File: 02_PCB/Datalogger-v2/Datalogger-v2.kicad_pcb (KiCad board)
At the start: 2 copper layers, 140 x 90 mm, 23 parts, among them U1 Micro SD Card Adapter, U7 TP4056, U8 ESP32 DEV KIT DOIT

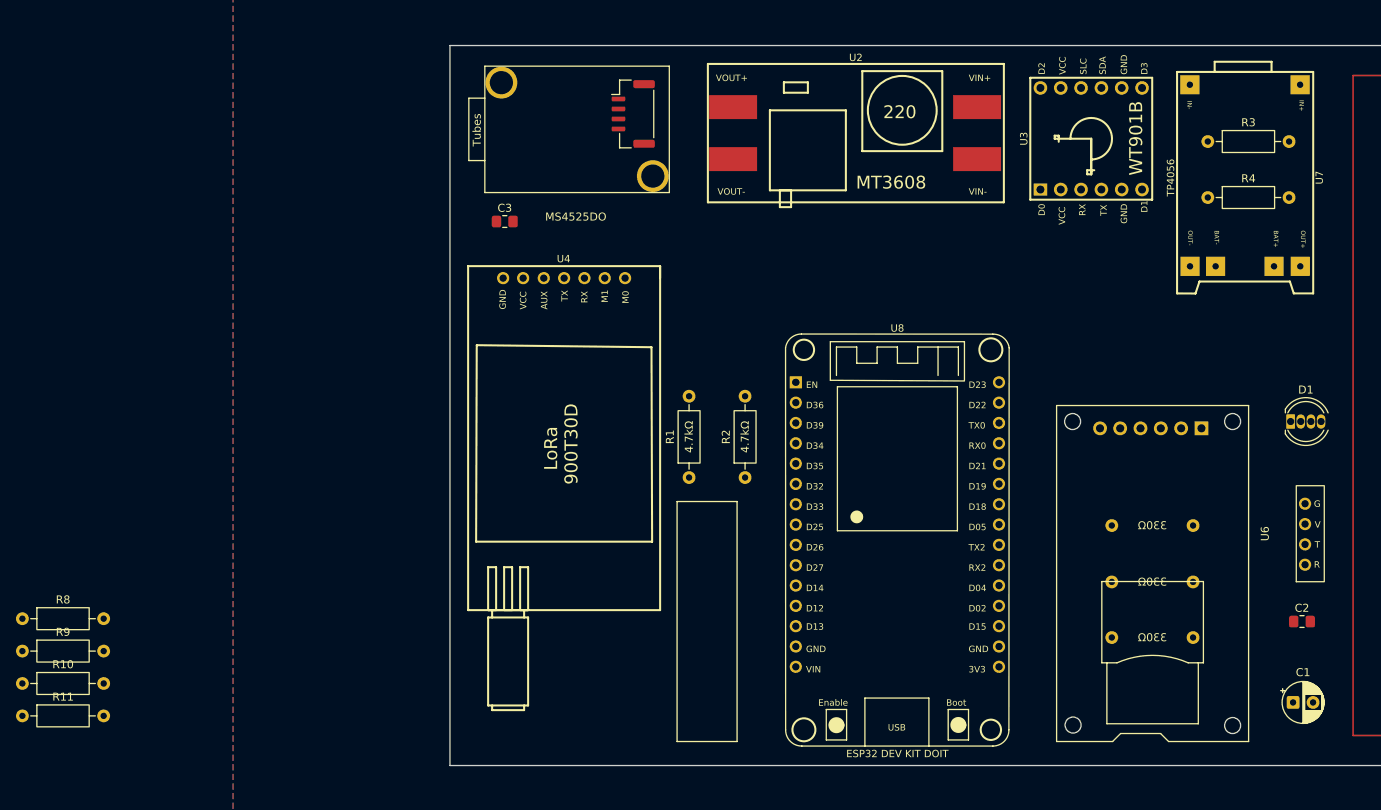
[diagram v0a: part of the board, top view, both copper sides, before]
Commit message: Update schematic and PCB files
- Add symbol and footprint library.
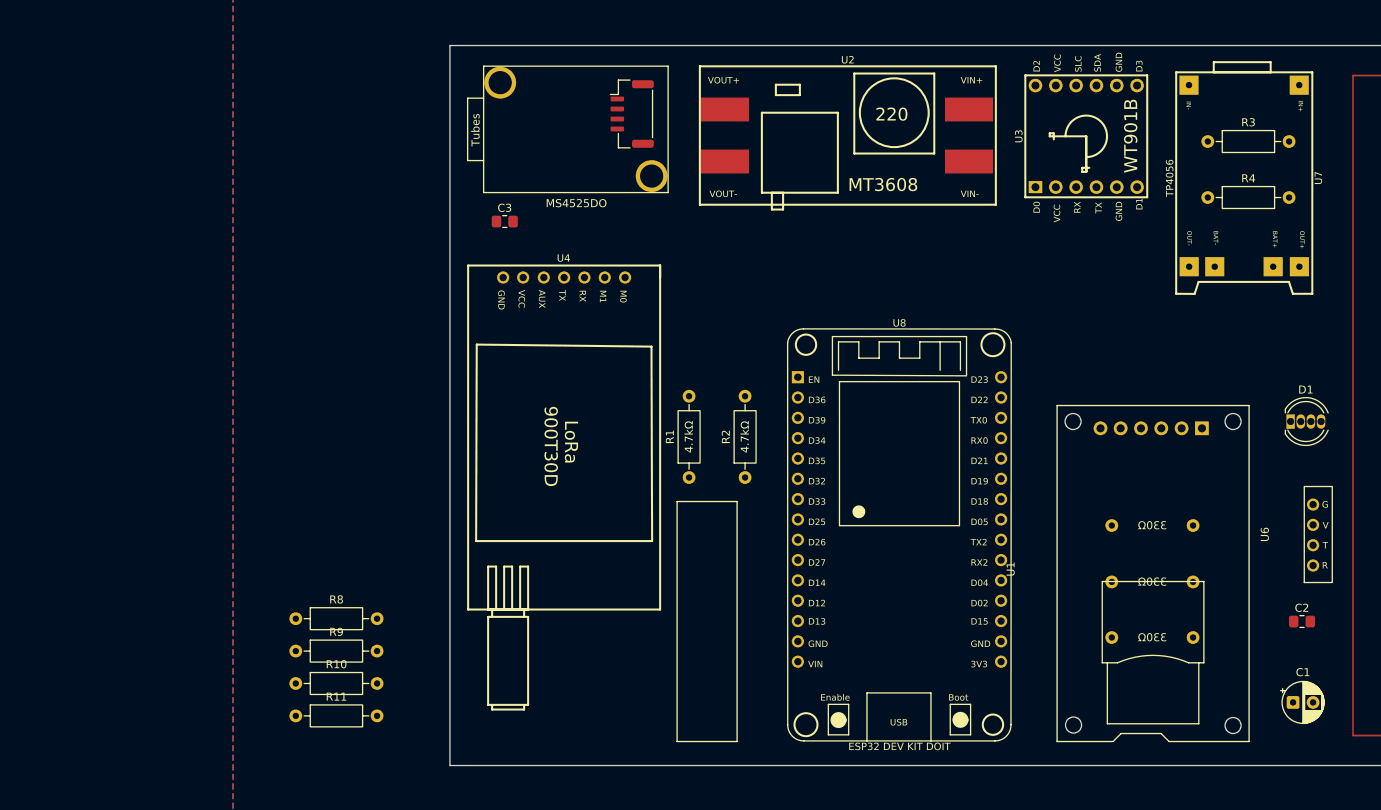
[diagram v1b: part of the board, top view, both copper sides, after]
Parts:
- U1: footprint New_Datalogger:Micro_SD_Adapter -> Datalogger-v2:Micro_SD_Adapter
- U2: footprint New_Datalogger:MT3608 -> Datalogger-v2:MT3608
- U3: footprint New_Datalogger:WT901B -> Datalogger-v2:WT901B
- U4: footprint New_Datalogger:E22-900T30D -> Datalogger-v2:E22-900T30D
- U5: footprint New_Datalogger:MS4525DO -> Datalogger-v2:MS4525DO
- U6: footprint New_Datalogger:GPS GEP-M10 -> Datalogger-v2:GPS GEP-M10
- U7: footprint New_Datalogger:TP4056 -> Datalogger-v2:TP4056
- U8: footprint New_Datalogger:DOIT-ESP32-DEVKIT-V1 -> Datalogger-v2:DOIT-ESP32-DEVKIT-V1
- moved R10 34.2 mm to (109.8, 180.7)
- moved R11 34.2 mm to (109.8, 184.8)
- moved R8 34.2 mm to (109.8, 172.6)
- moved R9 34.2 mm to (109.8, 176.7)
- moved U2 1.04 mm to (178.8, 112.3)
- moved U6 1.01 mm to (237.9, 162.1)
- moved U8 0.69 mm to (172.6, 142.5)
- moved U3 0.69 mm to (208.7, 112.5)
- moved U5 0.15 mm to (145.0, 126.0)
- moved U7 0.12 mm to (227.9, 117.0)
- moved U4 0.08 mm to (131.4, 128.5)
- moved U1 0.06 mm to (205.0, 188.0)
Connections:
- R5 pad 1: unconnected-(R5-Pad1) -> Net-(U8-LED0/D2)
- R6 pad 1: unconnected-(R6-Pad1) -> Net-(U8-ADC/D4)
- R7 pad 1: unconnected-(R7-Pad1) -> Net-(U8-D5)
- U4 pad 3: unconnected-(U4-RX-Pad3) -> Net-(U4-RX)
- U4 pad 4: unconnected-(U4-TX-Pad4) -> Net-(U4-TX)
- U6 pad 1: unconnected-(U6-RX-Pad1) -> Net-(U6-RX)
- U6 pad 2: unconnected-(U6-TX-Pad2) -> Net-(U6-TX)
- U8 pad 1: unconnected-(U8-3V3-Pad1) -> 5V/2A
- U8 pad 10: unconnected-(U8-ADC/D32-Pad10) -> Net-(U1-MISO)
- U8 pad 11: unconnected-(U8-ADC/D35*-Pad11) -> Net-(U3-SDA)
- U8 pad 12: unconnected-(U8-ADC/D34*-Pad12) -> Net-(U4-TX)
- U8 pad 13: unconnected-(U8-UA0TX/D1-Pad13) -> Net-(U4-RX)
- U8 pad 14: unconnected-(U8-D22-Pad14) -> Net-(U3-SCL)
- U8 pad 15: unconnected-(U8-D23-Pad15) -> Net-(U1-MOSI)
- U8 pad 2: unconnected-(U8-GND-Pad2) -> GND
- U8 pad 3: Net-(U8-ADC/D13) -> Net-(U1-CS)
- U8 pad 4: unconnected-(U8-ADC/D12-Pad4) -> Net-(U8-LED0/D2)
- U8 pad 7: unconnected-(U8-ADC/DAC1/D26-Pad7) -> Net-(U6-RX)
- U8 pad 8: unconnected-(U8-ADC/DAC0/D25-Pad8) -> Net-(U8-D5)
- U8 pad 9: unconnected-(U8-ADC/D33-Pad9) -> Net-(U1-SCK)

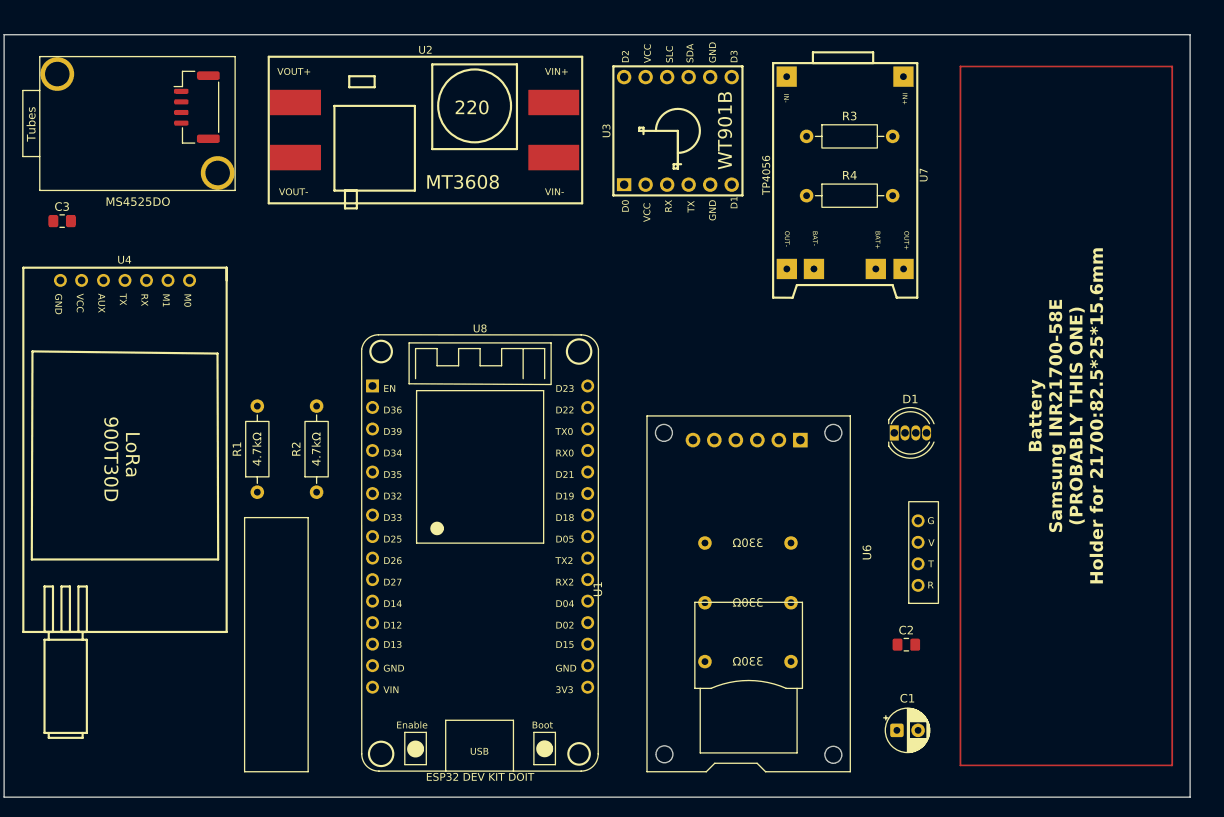
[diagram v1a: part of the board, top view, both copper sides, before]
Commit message: Update PCB file
- Fix design rules
- Add tracks
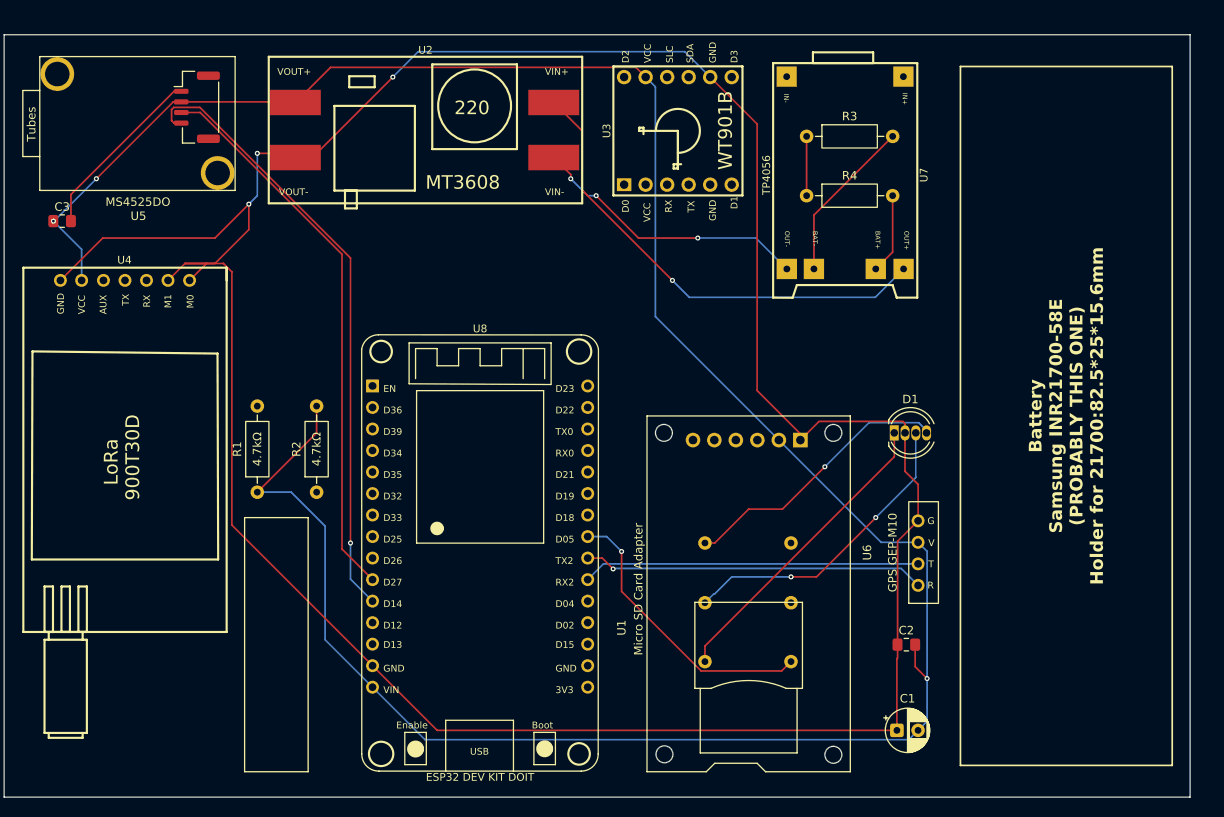
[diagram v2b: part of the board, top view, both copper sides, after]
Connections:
- U8 pad 1: 5V/2A -> unconnected-(U8-30-Pad1)
- U8 pad 10: Net-(U1-MISO) -> Net-(U5-SDA)
- U8 pad 11: Net-(U3-SDA) -> Net-(U5-SCL)
- U8 pad 12: Net-(U4-TX) -> unconnected-(U8-ADC/D12-Pad12)
- U8 pad 13: Net-(U4-RX) -> Net-(U8-ADC/D13)
- U8 pad 14: Net-(U3-SCL) -> GND
- U8 pad 15: Net-(U1-MOSI) -> 5V/2A
- U8 pad 16: (no net) -> Net-(U1-MOSI)
- U8 pad 17: (no net) -> Net-(U3-SCL)
- U8 pad 18: (no net) -> Net-(U4-RX)
- U8 pad 19: (no net) -> Net-(U4-TX)
- U8 pad 2: GND -> unconnected-(U8-29-Pad2)
- U8 pad 20: (no net) -> Net-(U3-SDA)
- U8 pad 21: (no net) -> Net-(U1-MISO)
- U8 pad 22: (no net) -> Net-(U1-SCK)
- U8 pad 23: (no net) -> Net-(U8-D5)
- U8 pad 24: (no net) -> Net-(U6-RX)
- U8 pad 25: (no net) -> Net-(U6-TX)
- U8 pad 26: (no net) -> Net-(U8-ADC/D4)
- U8 pad 27: (no net) -> Net-(U8-LED0/D2)
- U8 pad 28: (no net) -> Net-(U1-CS)
- U8 pad 3: Net-(U1-CS) -> unconnected-(U8-VN_(ADC/D39*)-Pad3)
- U8 pad 4: Net-(U8-LED0/D2) -> unconnected-(U8-ADC/D34*-Pad4)
- U8 pad 5: Net-(U5-SCL) -> unconnected-(U8-ADC/D35*-Pad5)
- U8 pad 6: Net-(U5-SDA) -> unconnected-(U8-ADC/D32-Pad6)
- U8 pad 7: Net-(U6-RX) -> unconnected-(U8-ADC/D33-Pad7)
- U8 pad 8: Net-(U8-D5) -> unconnected-(U8-ADC/DAC0/D25-Pad8)
- U8 pad 9: Net-(U1-SCK) -> unconnected-(U8-ADC/DAC1/D26-Pad9)
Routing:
- net GND: track 0.00 -> 333.2 mm, vias 0 -> 3
- net 5V/2A: track 0.00 -> 296.3 mm, vias 0 -> 3
- net Net-(U5-SCL): track 0.00 -> 72.7 mm, vias 0 -> 1
- net Net-(U5-SDA): track 0.00 -> 65.8 mm
- net Net-(U2-VIN+): track 0.00 -> 56.3 mm, vias 0 -> 1
- net Net-(U6-RX): track 0.00 -> 40.4 mm, vias 0 -> 1
- net Net-(U6-TX): track 0.00 -> 39.8 mm
- net Net-(D1-VDD): track 0.00 -> 36.3 mm, vias 0 -> 2
- net Net-(D1-DO): track 0.00 -> 36.3 mm
- net Net-(U8-D5): track 0.00 -> 33.8 mm, vias 0 -> 1
- net Net-(U2-VIN-): track 0.00 -> 33.2 mm, vias 0 -> 3
- net Net-(D1-DI): track 0.00 -> 32.7 mm, vias 0 -> 1
- net Net-(U5-GND): track 0.00 -> 21.2 mm
- net Net-(BT1--): track 0.00 -> 19.5 mm
- net Net-(BT1-+): track 0.00 -> 9.47 mm
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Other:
- board text added: "Keep in mind for LoRa: power routing must be avoided under the module (top or bottom layer)."

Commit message: Update PCB file
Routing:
- net Net-(U3-SDA): track 0.00 -> 95.2 mm
- net Net-(U8-ADC/D13): track 7.00 -> 88.4 mm, vias 0 -> 2
- net Net-(U3-SCL): track 0.00 -> 81.0 mm, vias 0 -> 2
- net Net-(U4-TX): track 0.00 -> 65.4 mm
- net Net-(U4-RX): track 0.00 -> 61.0 mm, vias 0 -> 2
- net Net-(U1-CS): track 0.00 -> 29.4 mm
- net Net-(U8-LED0/D2): track 0.00 -> 27.9 mm, vias 0 -> 1
- net Net-(U8-ADC/D4): track 0.00 -> 25.7 mm, vias 0 -> 2
- net Net-(U1-MISO): track 0.00 -> 23.6 mm
- net Net-(U1-MOSI): track 0.00 -> 20.1 mm
- net Net-(U1-SCK): track 0.00 -> 18.6 mm
- net GND: track 333.2 -> 322.2 mm

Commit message: Update schematic and PCB files
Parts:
- R10, R11, R8, R9: moved to B.Cu
- moved R10 137.0 mm to (239.0, 134.9), turned to -90 degrees
- moved R11 132.9 mm to (233.0, 134.8), turned to -90 degrees
- moved R8 131.5 mm to (239.0, 147.9), turned to -90 degrees
- moved R9 126.5 mm to (233.0, 147.9), turned to -90 degrees
- moved R7 25.1 mm to (212.0, 152.0), turned to -90 degrees
- moved R6 16.8 mm to (217.0, 152.0), turned to -90 degrees
- moved D1 15.8 mm to (222.0, 138.0)
- moved R5 9.00 mm to (222.0, 152.0), turned to -90 degrees
- moved U6 4.12 mm to (236.9, 166.1)
- moved C2 3.00 mm to (235.6, 176.0)
- moved C1 0.66 mm to (234.5, 183.8)
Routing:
- net 5V/2A: track 296.3 -> 187.7 mm, vias 3 -> 2
- net Net-(U6-RX): track 40.4 -> 0.00 mm, vias 1 -> 0
- net Net-(U6-TX): track 39.8 -> 0.00 mm
- net Net-(D1-VDD): track 36.3 -> 0.00 mm, vias 2 -> 0
- net Net-(D1-DO): track 36.3 -> 0.00 mm
- net Net-(D1-DI): track 32.7 -> 0.00 mm, vias 1 -> 0
- net Net-(U8-D5): track 33.8 -> 17.4 mm, vias 1 -> 0
- net GND: track 322.2 -> 307.6 mm
- net Net-(U8-LED0/D2): track 27.9 -> 31.6 mm
- net Net-(U1-SCK): track 18.6 -> 18.7 mm, vias 0 -> 1

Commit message: Update PCB schematic
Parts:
- moved D1 49.1 mm to (174.2, 127.0)
- moved R5 36.7 mm to (198.0, 124.2)
- moved R10 33.8 mm to (211.8, 155.0), turned to 0 degrees
- moved R7 31.3 mm to (193.2, 127.0), turned to 180 degrees
- moved R6 31.1 mm to (193.2, 132.0), turned to 180 degrees
- moved R8 30.6 mm to (211.8, 162.0), turned to 0 degrees
- moved U6 26.1 mm to (229.3, 141.1), turned to 0 degrees
- moved R11 25.3 mm to (236.0, 160.0)
- moved R9 3.61 mm to (236.0, 145.9)
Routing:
- net 5V/2A: track 187.7 -> 250.0 mm
- net Net-(U6-TX): track 0.00 -> 47.9 mm
- net Net-(U6-RX): track 0.00 -> 40.0 mm
- net Net-(U1-CS): track 29.4 -> 62.0 mm
- net Net-(D1-DI): track 0.00 -> 23.1 mm
- net Net-(U1-MISO): track 23.6 -> 43.6 mm, vias 0 -> 2
- net Net-(U8-LED0/D2): track 31.6 -> 49.5 mm, vias 1 -> 0
- net Net-(U8-D5): track 17.4 -> 35.2 mm
- net GND: track 307.6 -> 324.7 mm, vias 3 -> 4
- net Net-(U8-ADC/D4): track 25.6 -> 37.9 mm, vias 2 -> 0
- net Net-(U1-SCK): track 18.7 -> 30.4 mm
- net Net-(D1-DO): track 0.00 -> 10.7 mm
- net Net-(D1-VDD): track 0.00 -> 8.77 mm
- net Net-(U3-SCL): track 81.0 -> 84.4 mm, vias 2 -> 5
- net Net-(U3-SDA): vias 0 -> 1

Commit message: Update schematic
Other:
- board text added: "Next step: compare constraints of past Datalogger's PCB with this one. Just copy and paste the values. Specifically the vias holes?? (Just anything)"
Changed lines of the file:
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@@
 				(font
 					(size 1.27 1.27)
-					(thickness 0.15)
 				)
 			)
@@
 				(font
 					(size 1.27 1.27)
-					(thickness 0.15)
 				)
 			)
@@
 		(sheetname "/")
 		(sheetfile "Datalogger-v2.kicad_sch")
-		(units
-			(unit
-				(name "A")
-				(pins "1" "2" "3" "4" "5" "6" "7" "8" "9" "10" "11" "12" "13" "14" "15"
-					"16" "17" "18" "19" "20" "21" "22" "23" "24" "25" "26" "27" "28"
-				)
-			)
-		)
 		(duplicate_pad_numbers_are_jumpers no)
 		(fp_line
@@
 				(bold yes)
 			)
+			(justify left bottom)
+		)
+	)
+	(gr_text "Next step: compare constraints of past Datalogger's PCB with this one. \nJust copy and paste the values. \nSpecifically the vias holes?? \n(Just anything)"
+		(at 112 154 0)
+		(layer "Cmts.User")
+		(effects
+			(font
+				(size 1.5 1.5)
+				(thickness 0.3)
+				(bold yes)
+			)
